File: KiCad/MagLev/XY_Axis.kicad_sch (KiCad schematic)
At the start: 26 parts, among them Q1 ZX5T851GTA, Q2 ZX5T1951GTA, Q3 ZX5T851GTA, Q4 ZX5T1951GTA, U1 LM324

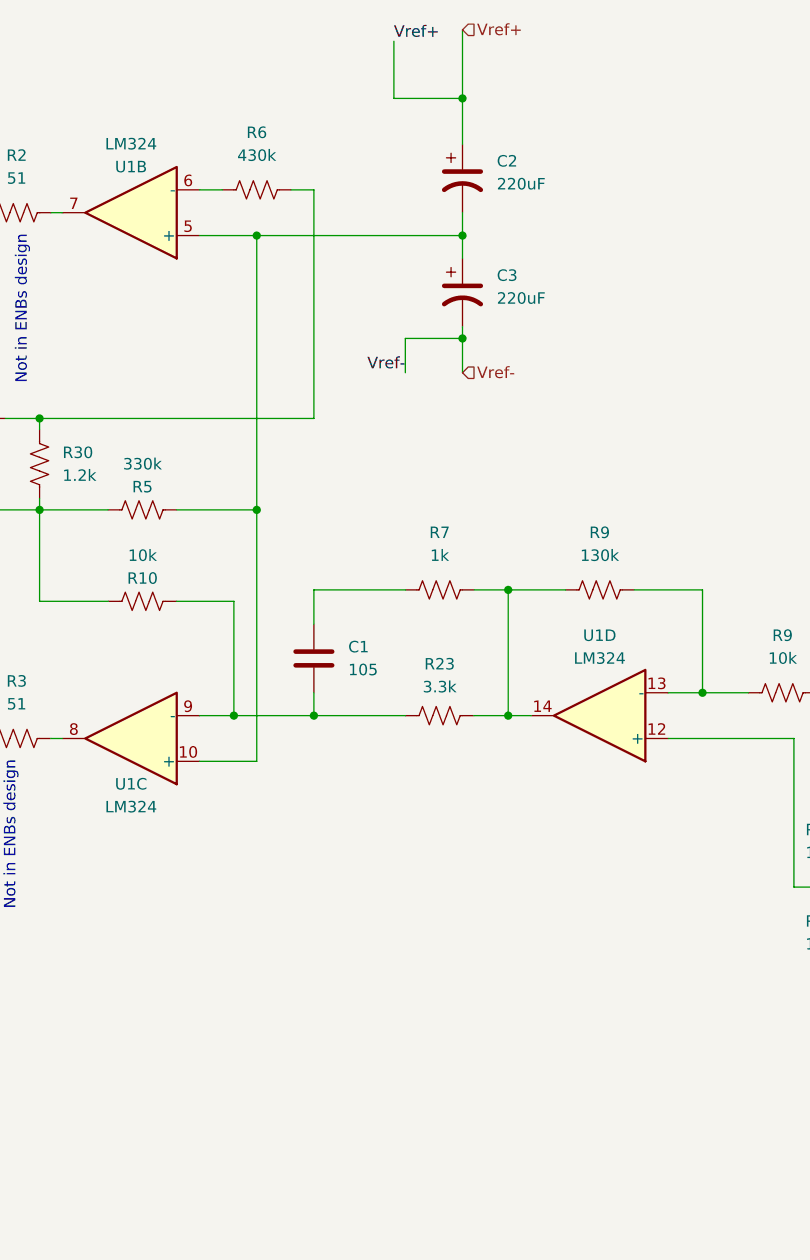
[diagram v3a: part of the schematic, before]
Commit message: Update spice model to match enbs design. Add TVS diodes to schematic.
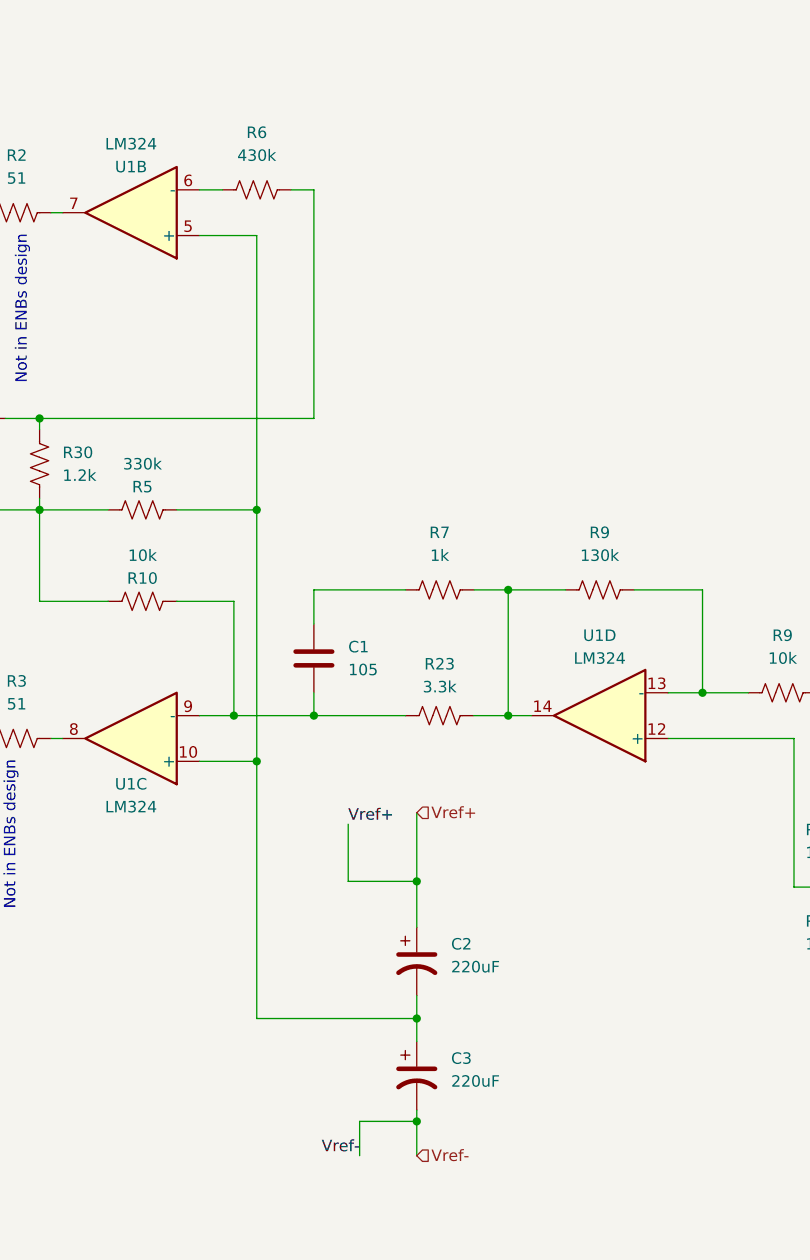
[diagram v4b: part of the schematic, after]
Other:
- moved on the sheet: C2, C3
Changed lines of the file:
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@@
   (junction (at 105.41 119.38) (diameter 0) (color 0 0 0 0)
   )
-  (junction (at 147.32 63.5) (diameter 0) (color 0 0 0 0)
-  )
   (junction (at 73.66 119.38) (diameter 0) (color 0 0 0 0)
   )
@@
   (junction (at 105.41 135.89) (diameter 0) (color 0 0 0 0)
   )
-  (junction (at 170.18 74.93) (diameter 0) (color 0 0 0 0)
+  (junction (at 165.1 161.925) (diameter 0) (color 0 0 0 0)
+  )
+  (junction (at 147.32 121.92) (diameter 0) (color 0 0 0 0)
   )
   (junction (at 153.67 116.84) (diameter 0) (color 0 0 0 0)
@@
   (junction (at 86.36 60.96) (diameter 0) (color 0 0 0 0)
   )
-  (junction (at 170.18 48.26) (diameter 0) (color 0 0 0 0)
-  )
-  (junction (at 170.18 63.5) (diameter 0) (color 0 0 0 0)
+  (junction (at 165.1 135.255) (diameter 0) (color 0 0 0 0)
+  )
+  (junction (at 165.1 150.495) (diameter 0) (color 0 0 0 0)
   )
   (junction (at 114.3 60.96) (diameter 0) (color 0 0 0 0)
@@
     (stroke (width 0) (type default))
   )
-  (wire (pts (xy 170.18 63.5) (xy 170.18 66.04))
+  (wire (pts (xy 165.1 150.495) (xy 165.1 153.035))
     (stroke (width 0) (type default))
   )
@@
     (stroke (width 0) (type default))
   )
-  (wire (pts (xy 170.18 48.26) (xy 170.18 53.34))
+  (wire (pts (xy 165.1 135.255) (xy 165.1 140.335))
     (stroke (width 0) (type default))
   )
@@
     (stroke (width 0) (type default))
   )
-  (wire (pts (xy 163.83 74.93) (xy 170.18 74.93))
+  (wire (pts (xy 158.75 161.925) (xy 165.1 161.925))
     (stroke (width 0) (type default))
   )
@@
     (stroke (width 0) (type default))
   )
-  (wire (pts (xy 170.18 60.96) (xy 170.18 63.5))
-    (stroke (width 0) (type default))
-  )
-  (wire (pts (xy 162.56 48.26) (xy 162.56 41.91))
-    (stroke (width 0) (type default))
-  )
-  (wire (pts (xy 170.18 74.93) (xy 170.18 78.74))
+  (wire (pts (xy 165.1 147.955) (xy 165.1 150.495))
+    (stroke (width 0) (type default))
+  )
+  (wire (pts (xy 157.48 135.255) (xy 157.48 128.905))
+    (stroke (width 0) (type default))
+  )
+  (wire (pts (xy 165.1 161.925) (xy 165.1 165.735))
     (stroke (width 0) (type default))
   )
@@
     (stroke (width 0) (type default))
   )
+  (wire (pts (xy 147.32 150.495) (xy 147.32 121.92))
+    (stroke (width 0) (type default))
+  )
   (wire (pts (xy 86.36 115.57) (xy 86.36 119.38))
     (stroke (width 0) (type default))
@@
     (stroke (width 0) (type default))
   )
-  (wire (pts (xy 147.32 63.5) (xy 170.18 63.5))
+  (wire (pts (xy 147.32 150.495) (xy 165.1 150.495))
     (stroke (width 0) (type default))
   )
@@
     (stroke (width 0) (type default))
   )
-  (wire (pts (xy 170.18 48.26) (xy 162.56 48.26))
+  (wire (pts (xy 165.1 135.255) (xy 157.48 135.255))
     (stroke (width 0) (type default))
   )
@@
     (stroke (width 0) (type default))
   )
-  (wire (pts (xy 170.18 40.64) (xy 170.18 48.26))
+  (wire (pts (xy 165.1 127.635) (xy 165.1 135.255))
     (stroke (width 0) (type default))
   )
@@
     (stroke (width 0) (type default))
   )
-  (wire (pts (xy 163.83 78.74) (xy 163.83 74.93))
+  (wire (pts (xy 158.75 165.735) (xy 158.75 161.925))
     (stroke (width 0) (type default))
   )
@@
     (stroke (width 0) (type default))
   )
-  (wire (pts (xy 170.18 73.66) (xy 170.18 74.93))
+  (wire (pts (xy 165.1 160.655) (xy 165.1 161.925))
     (stroke (width 0) (type default))
   )
@@
     (effects (font (size 1.27 1.27)) (justify left bottom))
   )
-  (label "Vref+" (at 162.56 41.91 0) (fields_autoplaced)
+  (label "Vref+" (at 157.48 128.905 0) (fields_autoplaced)
     (effects (font (size 1.27 1.27)) (justify left bottom))
   )
-  (label "Vref-" (at 163.83 78.74 180) (fields_autoplaced)
+  (label "Vref-" (at 158.75 165.735 180) (fields_autoplaced)
     (effects (font (size 1.27 1.27)) (justify right bottom))
   )
@@
     (effects (font (size 1.27 1.27)) (justify left))
   )
-  (hierarchical_label "Vref-" (shape input) (at 170.18 78.74 0) (fields_autoplaced)
+  (hierarchical_label "Vref-" (shape input) (at 165.1 165.735 0) (fields_autoplaced)
     (effects (font (size 1.27 1.27)) (justify left))
   )
-  (hierarchical_label "Vref+" (shape input) (at 170.18 40.64 0) (fields_autoplaced)
+  (hierarchical_label "Vref+" (shape input) (at 165.1 127.635 0) (fields_autoplaced)
     (effects (font (size 1.27 1.27)) (justify left))
   )
@@
     )
   )
-  (symbol (lib_id "Device:C_Polarized_US") (at 170.18 69.85 0) (unit 1)
-    (in_bom yes) (on_board yes) (dnp no) (fields_autoplaced)
-    (property "Reference" "C3" (at 173.99 67.945 0)
-      (effects (font (size 1.27 1.27)) (justify left))
-    )
-    (property "Value" "220uF" (at 173.99 70.485 0)
-      (effects (font (size 1.27 1.27)) (justify left))
-    )
-    (property "Footprint" "Capacitor_SMD:CP_Elec_8x10" (at 170.18 69.85 0)
-      (effects (font (size 1.27 1.27)) hide)
-    )
-    (property "Datasheet" "~" (at 170.18 69.85 0)
+  (symbol (lib_id "Device:C_Polarized_US") (at 165.1 156.845 0) (unit 1)
+    (in_bom yes) (on_board yes) (dnp no) (fields_autoplaced)
+    (property "Reference" "C3" (at 168.91 154.94 0)
+      (effects (font (size 1.27 1.27)) (justify left))
+    )
+    (property "Value" "220uF" (at 168.91 157.48 0)
+      (effects (font (size 1.27 1.27)) (justify left))
+    )
+    (property "Footprint" "Capacitor_SMD:CP_Elec_8x10" (at 165.1 156.845 0)
+      (effects (font (size 1.27 1.27)) hide)
+    )
+    (property "Datasheet" "~" (at 165.1 156.845 0)
       (effects (font (size 1.27 1.27)) hide)
     )
@@
     )
   )
-  (symbol (lib_id "Device:C_Polarized_US") (at 170.18 57.15 0) (unit 1)
-    (in_bom yes) (on_board yes) (dnp no) (fields_autoplaced)
-    (property "Reference" "C2" (at 173.99 55.245 0)
-      (effects (font (size 1.27 1.27)) (justify left))
-    )
-    (property "Value" "220uF" (at 173.99 57.785 0)
-      (effects (font (size 1.27 1.27)) (justify left))
-    )
-    (property "Footprint" "Capacitor_SMD:CP_Elec_8x10" (at 170.18 57.15 0)
-      (effects (font (size 1.27 1.27)) hide)
-    )
-    (property "Datasheet" "~" (at 170.18 57.15 0)
-      (effects (font (size 1.27 1.27)) hide)
-    )
+  (symbol (lib_id "Device:C_Polarized_US") (at 165.1 144.145 0) (unit 1)
+    (in_bom yes) (on_board yes) (dnp no) (fields_autoplaced)
+    (property "Reference" "C2" (at 168.91 142.24 0)
+      (effects (font (size 1.27 1.27)) (justify left))
+    )
+    (property "Value" "220uF" (at 168.91 144.78 0)
+      (effects (font (size 1.27 1.27)) (justify left))
+    )
+    (property "Footprint" "Capacitor_SMD:CP_Elec_8x10" (at 165.1 144.145 0)
+      (effects (font (size 1.27 1.27)) hide)
+    )
+    (property "Datasheet" "~" (at 165.1 144.145 0)
+      (effects (font (size 1.27 1.27)) hide)
+    )

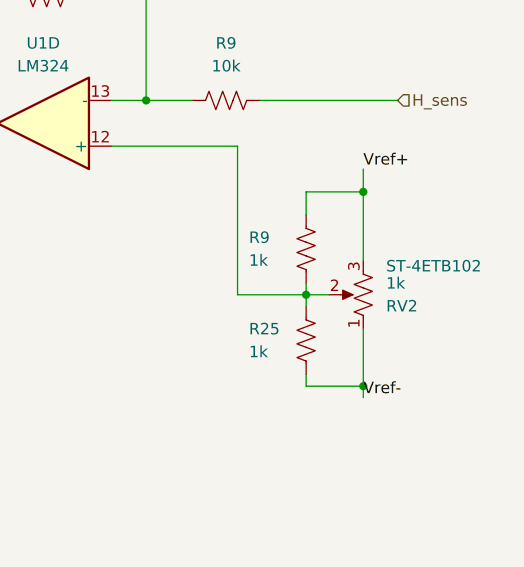
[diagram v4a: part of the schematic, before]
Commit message: Add MCU page to schematic.
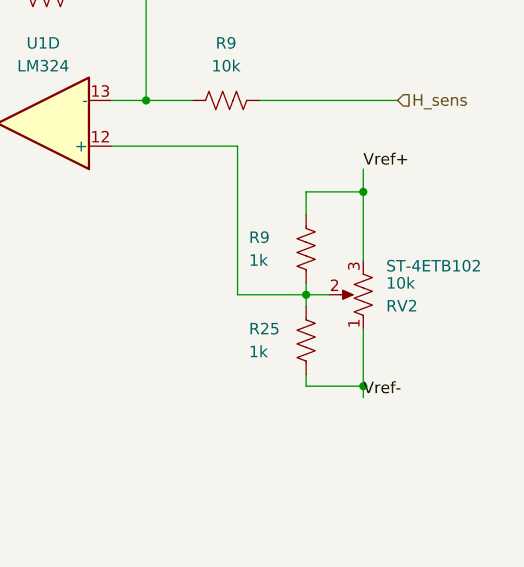
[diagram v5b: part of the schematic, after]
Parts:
- RV2: value 1k -> 10k
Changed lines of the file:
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@@
       (effects (font (size 1.27 1.27)) (justify right))
     )
-    (property "Value" "1k" (at 223.52 134.62 0)
+    (property "Value" "10k" (at 223.52 134.62 0)
       (effects (font (size 1.27 1.27)) (justify right))
     )

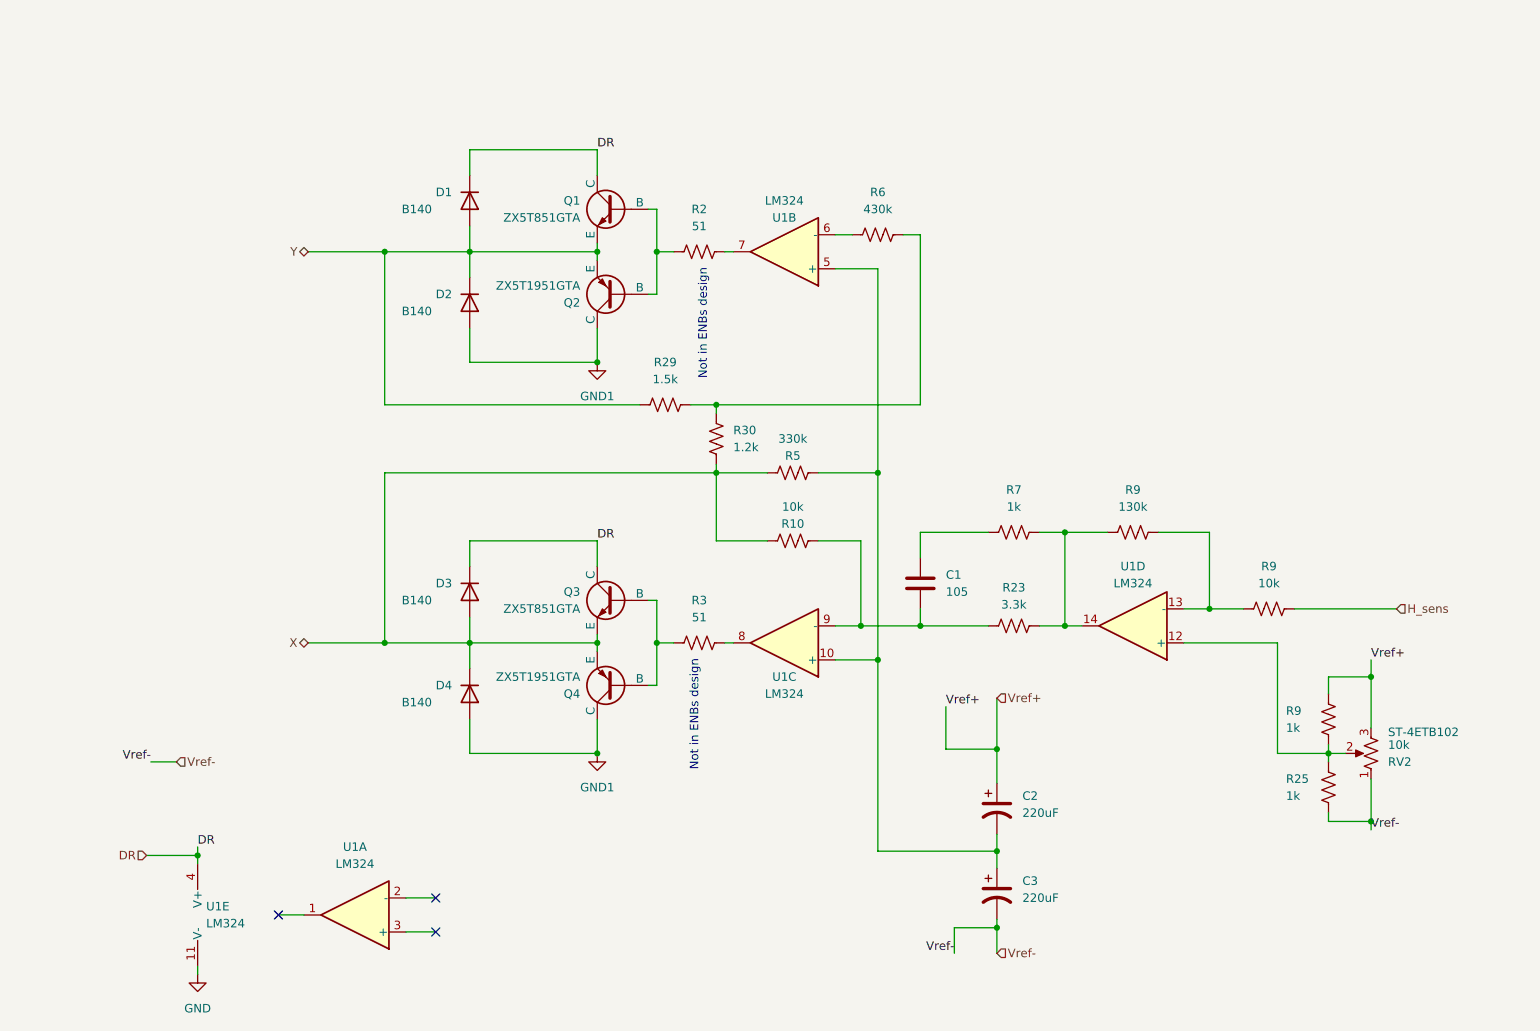
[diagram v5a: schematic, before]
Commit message: Add MCU and FTDI IC to schematic.
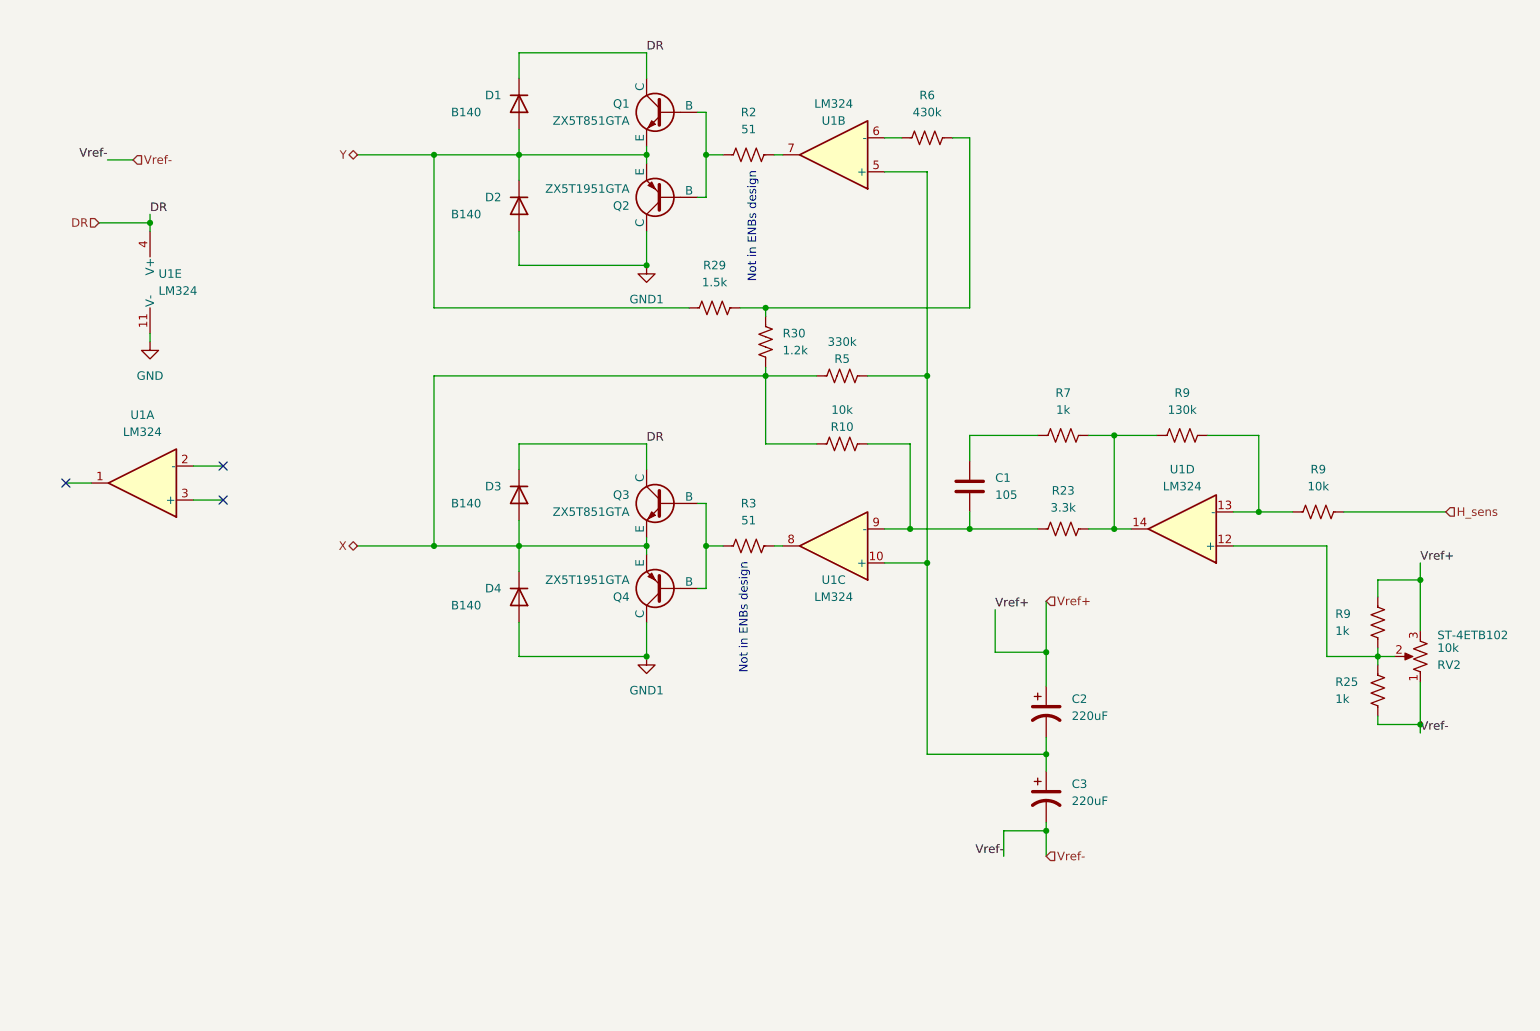
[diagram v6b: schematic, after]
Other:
- moved on the sheet: C1, C2, C3, D1, D2, D3, D4, Q1, Q2, Q3, Q4, R10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

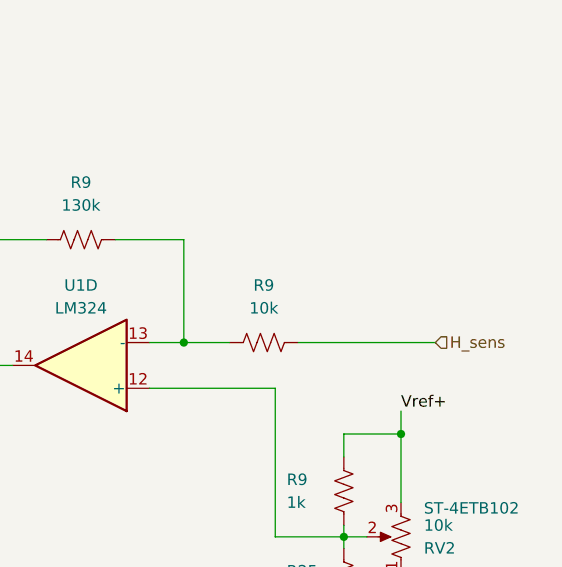
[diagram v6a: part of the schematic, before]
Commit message: Add power fets and additional coils to schematic.
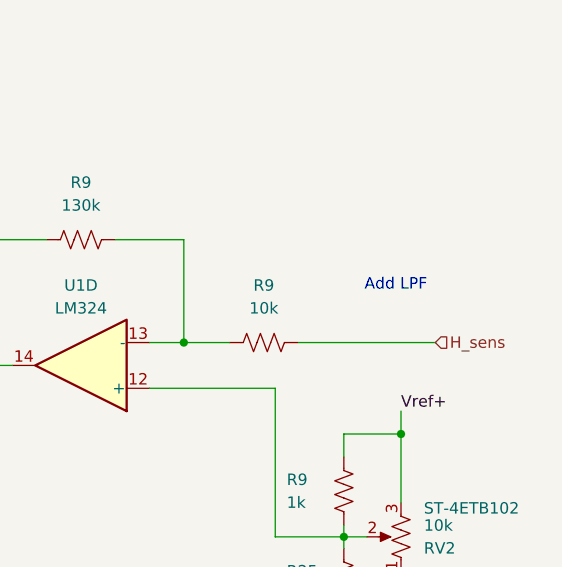
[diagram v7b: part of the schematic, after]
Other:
- note added: "Add LPF"
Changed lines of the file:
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@@
     (effects (font (size 1.27 1.27)) (justify right bottom))
+  )
+  (text "Add LPF" (at 224.282 94.234 0)
+    (effects (font (size 1.27 1.27)) (justify left bottom))
   )
   (label "DR" (at 112.776 89.662 0) (fields_autoplaced)
